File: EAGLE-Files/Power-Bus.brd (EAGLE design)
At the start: 36.8 x 9.8 mm, 13 parts

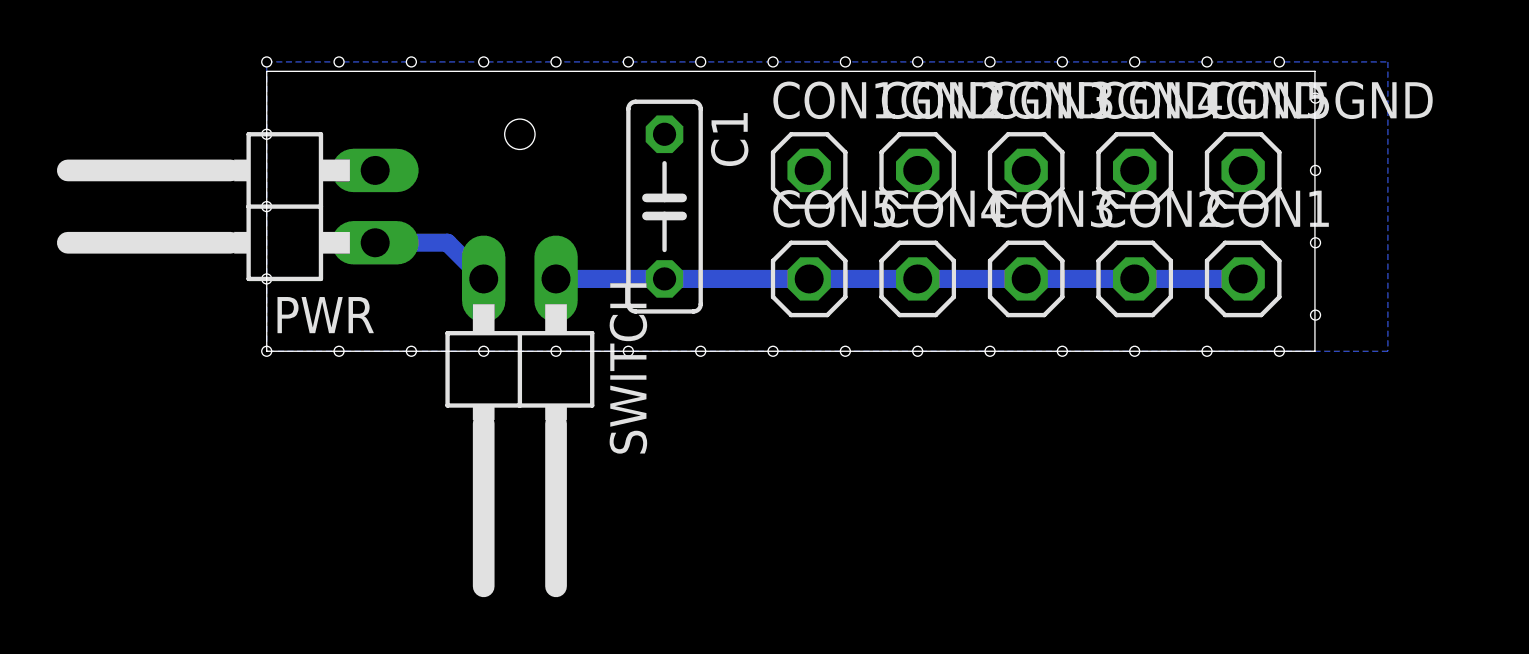
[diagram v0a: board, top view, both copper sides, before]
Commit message: Updated all boards for JLCPCB order
Also added the controller boards and schematics back
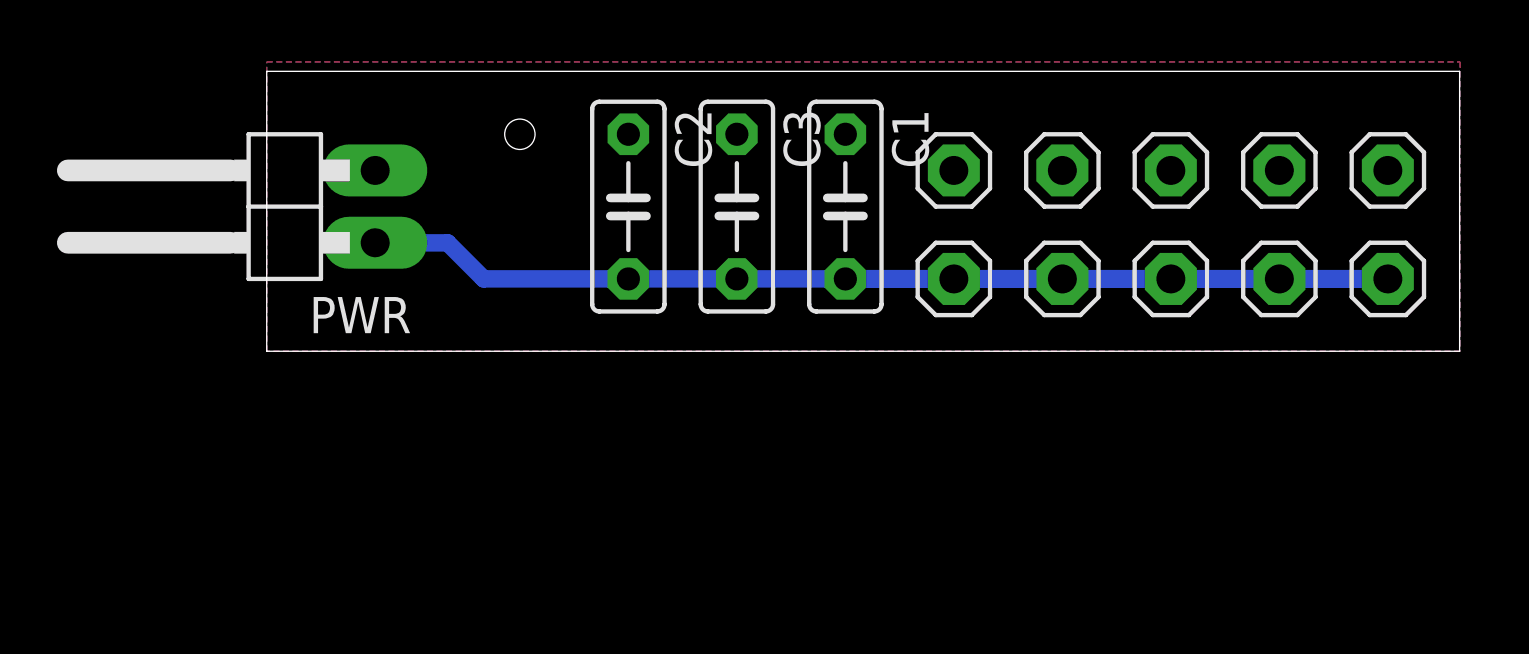
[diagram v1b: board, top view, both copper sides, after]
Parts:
- removed SWITCH: (no value), pinhead:1X02/90
- added C2, C3: (no value), rcl:C050-025X075
- moved C1 6.35 mm to (20.3, 5.08)
- moved CON2 5.08 mm to (35.6, 2.54)
- moved CON2GND 5.08 mm to (27.9, 6.35)
- moved CON4 5.08 mm to (27.9, 2.54)
- moved CON4GND 5.08 mm to (35.6, 6.35)
- moved CON1 5.08 mm to (39.4, 2.54)
- moved CON1GND 5.08 mm to (24.1, 6.35)
- moved CON3 5.08 mm to (31.8, 2.54)
- moved CON3GND 5.08 mm to (31.8, 6.35)
- moved CON5 5.08 mm to (24.1, 2.54)
- moved CON5GND 5.08 mm to (39.4, 6.35)
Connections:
- removed net 5VSWITCH: PWR.1, SWITCH.2
- net 5V: now also C2.2, C3.2, PWR.1; no longer SWITCH.1
- net GND: now also C2.1, C3.1
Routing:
- net 5V: track 24.1 -> 36.1 mm
- net 5VSWITCH: track 4.34 -> 0.00 mm
- added copper zone on layer 1, net GND
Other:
- board size 36.8 x 9.8 mm -> 41.9 x 9.8 mm
